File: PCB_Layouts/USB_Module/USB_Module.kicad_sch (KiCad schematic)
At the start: 3 parts, among them J1 USB_A, J2 Conn_01x10_Socket, J3 Conn_01x10_Socket

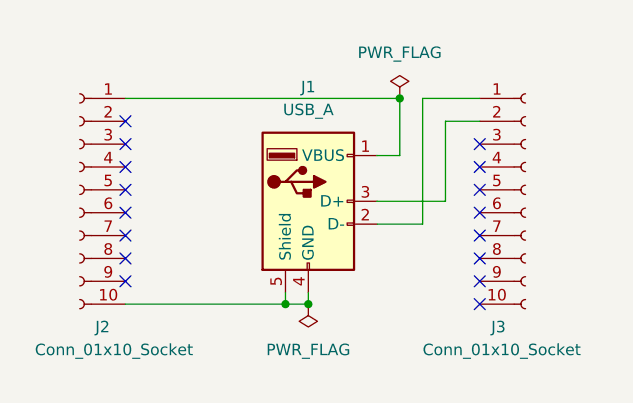
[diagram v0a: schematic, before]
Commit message: Updating modular interfaces module and quote
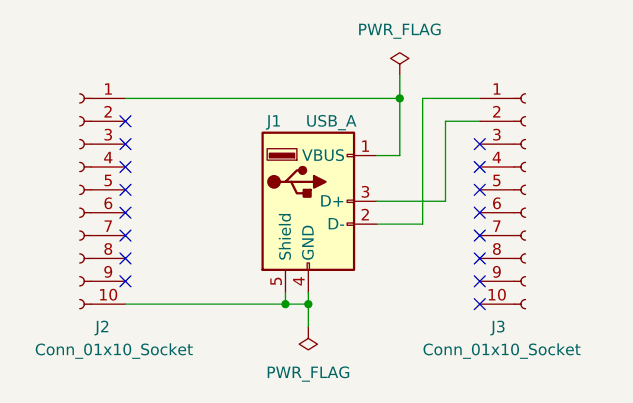
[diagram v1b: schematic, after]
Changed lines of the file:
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@@
+    (stroke (width 0) (type default))
+  )
+  (wire (pts (xy 121.92 101.6) (xy 121.92 99.06))
+    (stroke (width 0) (type default))
+  )
+  (wire (pts (xy 132.08 73.66) (xy 132.08 76.2))
     (stroke (width 0) (type default))
   )
@@
   (symbol (lib_id "Connector:USB_A") (at 121.92 87.63 0) (unit 1)
     (in_bom yes) (on_board yes) (dnp no)
-    (property "Reference" "J1" (at 121.92 74.93 0)
+    (property "Reference" "J1" (at 118.11 78.74 0)
       (effects (font (size 1.27 1.27)))
     )
-    (property "Value" "USB_A" (at 121.92 77.47 0)
+    (property "Value" "USB_A" (at 124.46 78.74 0)
       (effects (font (size 1.27 1.27)))
     )
@@
     )
   )
-  (symbol (lib_id "power:PWR_FLAG") (at 132.08 76.2 0) (unit 1)
+  (symbol (lib_id "power:PWR_FLAG") (at 132.08 73.66 0) (unit 1)
     (in_bom yes) (on_board yes) (dnp no) (fields_autoplaced)
-    (property "Reference" "#FLG02" (at 132.08 74.295 0)
+    (property "Reference" "#FLG02" (at 132.08 71.755 0)
       (effects (font (size 1.27 1.27)) hide)
     )
-    (property "Value" "PWR_FLAG" (at 132.08 71.12 0)
+    (property "Value" "PWR_FLAG" (at 132.08 68.58 0)
       (effects (font (size 1.27 1.27)))
     )
-    (property "Footprint" "" (at 132.08 76.2 0)
+    (property "Footprint" "" (at 132.08 73.66 0)
       (effects (font (size 1.27 1.27)) hide)
     )
-    (property "Datasheet" "~" (at 132.08 76.2 0)
+    (property "Datasheet" "~" (at 132.08 73.66 0)
       (effects (font (size 1.27 1.27)) hide)
     )
@@
     )
   )
-  (symbol (lib_id "power:PWR_FLAG") (at 121.92 99.06 180) (unit 1)
+  (symbol (lib_id "power:PWR_FLAG") (at 121.92 101.6 180) (unit 1)
     (in_bom yes) (on_board yes) (dnp no) (fields_autoplaced)
-    (property "Reference" "#FLG01" (at 121.92 100.965 0)
+    (property "Reference" "#FLG01" (at 121.92 103.505 0)
       (effects (font (size 1.27 1.27)) hide)
     )
-    (property "Value" "PWR_FLAG" (at 121.92 104.14 0)
+    (property "Value" "PWR_FLAG" (at 121.92 106.68 0)
       (effects (font (size 1.27 1.27)))
     )
-    (property "Footprint" "" (at 121.92 99.06 0)
+    (property "Footprint" "" (at 121.92 101.6 0)
       (effects (font (size 1.27 1.27)) hide)
     )
-    (property "Datasheet" "~" (at 121.92 99.06 0)
+    (property "Datasheet" "~" (at 121.92 101.6 0)
       (effects (font (size 1.27 1.27)) hide)
     )
